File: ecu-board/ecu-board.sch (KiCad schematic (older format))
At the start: 12 parts, among them J1 MicroSquirt_connector, J3 MS_breakout_conn, U1 MPX4250AP

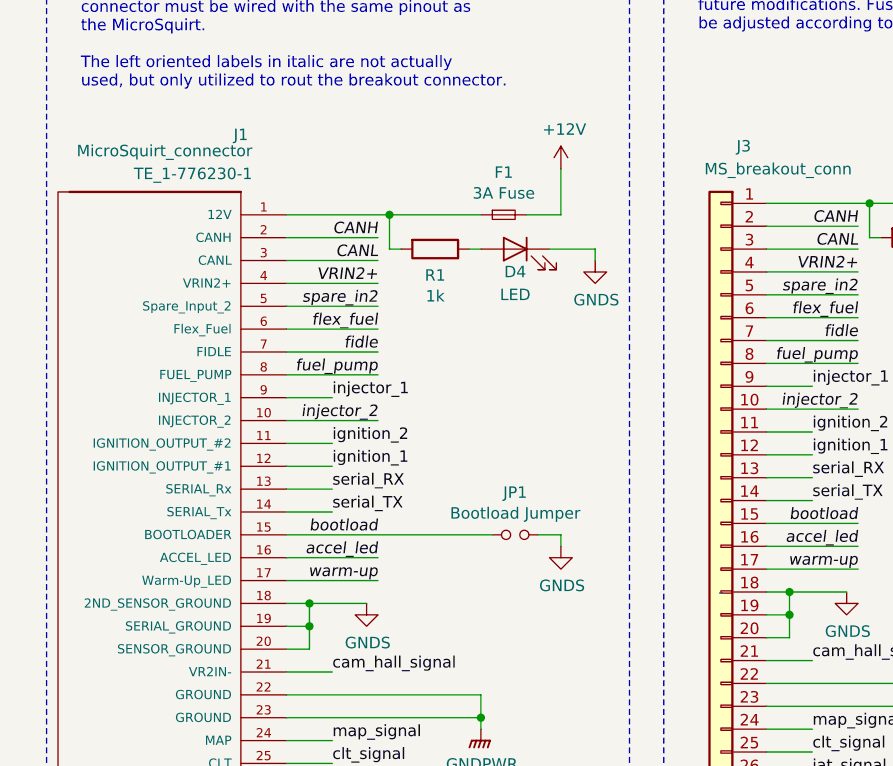
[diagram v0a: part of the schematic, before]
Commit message: Assign 2- and 3-pin terminal footprints.
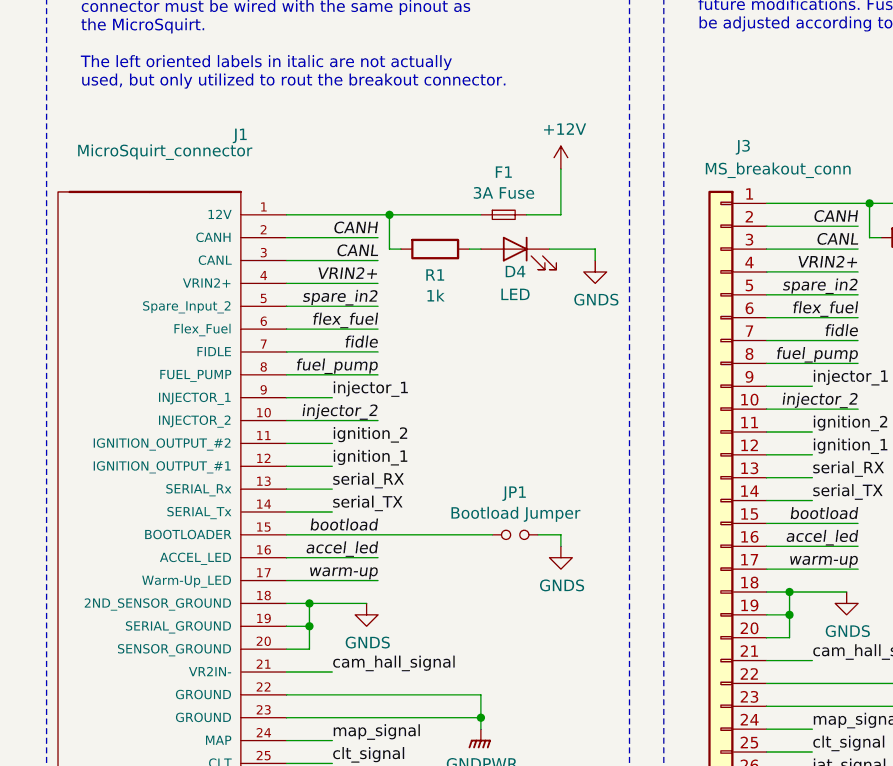
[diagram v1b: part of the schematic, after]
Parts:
- J1: footprint TE_1-776230-1 -> (none)
- J3: footprint - -> (none)
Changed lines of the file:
@@
 F 0 "J1" H 1650 6450 50  0000 C CNN
 F 1 "MicroSquirt_connector" H 1600 6350 50  0000 L BNN
-F 2 "TE_1-776230-1" H 1600 6250 50  0000 L BNN
+F 2 "" H 1600 6250 50  0000 L BNN
 F 3 "TE CONNECTIVITY" H 1850 4300 50  0001 L BNN
 	1    1850 4300
@@
 F 0 "J3" H 4050 6100 50  0000 C CNN
 F 1 "MS_breakout_conn" H 3900 6000 50  0000 C CNN
-F 2 "-" H 4150 4150 50  0000 C CNN
+F 2 "" H 4150 4150 50  0000 C CNN
 F 3 "https://www.phoenixcontact.com/gb/products/1791826" H 4150 4150 50  0001 C CNN
 F 4 "Phoenix Contact" H 4150 4150 50  0001 C CNN "Manufacturer"

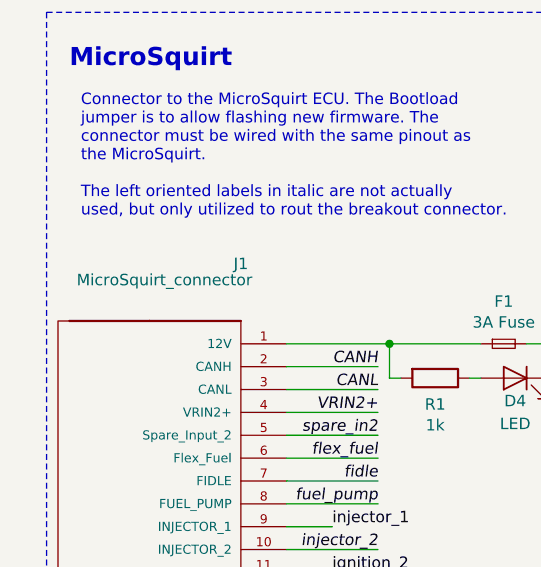
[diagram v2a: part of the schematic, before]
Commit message: Add component part no.
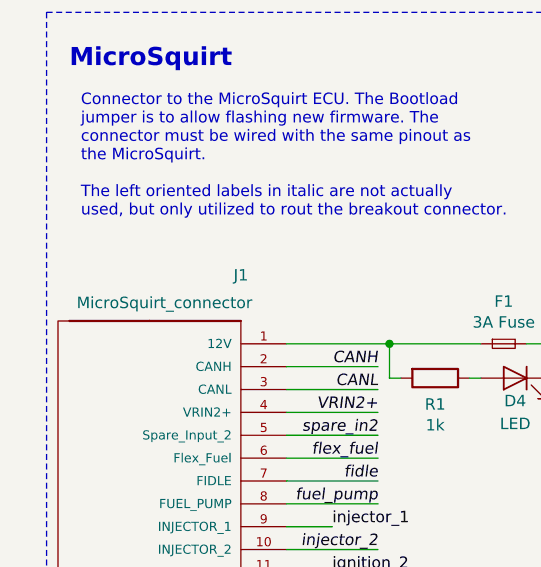
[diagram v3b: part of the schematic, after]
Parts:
- J1: Manufacturer (none) -> TE Connectivity; Part no. (none) -> 1-776230-1
- J3: Manufacturer Phoenix Contact -> (none)
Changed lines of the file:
@@
 U 1 1 5C598259
 P 1850 4300
-F 0 "J1" H 1650 6450 50  0000 C CNN
-F 1 "MicroSquirt_connector" H 1600 6350 50  0000 L BNN
+F 0 "J1" H 1650 6400 50  0000 C CNN
+F 1 "MicroSquirt_connector" H 1600 6250 50  0000 L BNN
 F 2 "" H 1600 6250 50  0001 L BNN
 F 3 "TE CONNECTIVITY" H 1850 4300 50  0001 L BNN
+F 4 "TE Connectivity" H 1850 4300 50  0001 C CNN "Manufacturer"
+F 5 "1-776230-1" H 1850 4300 50  0001 C CNN "Part no."
 	1    1850 4300
 	-1   0    0    -1
@@
 F 2 "" H 4150 4150 50  0001 C CNN
 F 3 "https://www.phoenixcontact.com/gb/products/1791826" H 4150 4150 50  0001 C CNN
-F 4 "Phoenix Contact" H 4150 4150 50  0001 C CNN "Manufacturer"
 	1    4150 4150
 	-1   0    0    -1

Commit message: Update LEDs.
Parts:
- D4, D5: Farnell 2251296 -> (none); Part no. (none) -> 3mm T-1
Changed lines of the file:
@@
 F 2 "LEDs:LED_D3.0mm" H 3250 2650 50  0001 C CNN
 F 3 "~" H 3250 2650 50  0001 C CNN
-F 4 "2251296" H 3250 2650 50  0001 C CNN "Farnell"
+F 4 "3mm T-1" H 3250 2650 50  0001 C CNN "Part no."
 	1    3250 2650
 	-1   0    0    -1
@@
 F 2 "LEDs:LED_D3.0mm" H 5350 2600 50  0001 C CNN
 F 3 "~" H 5350 2600 50  0001 C CNN
-F 4 "2251296" H 5350 2600 50  0001 C CNN "Farnell"
+F 4 "3mm T-1" H 5350 2600 50  0001 C CNN "Part no."
 	1    5350 2600
 	-1   0    0    -1

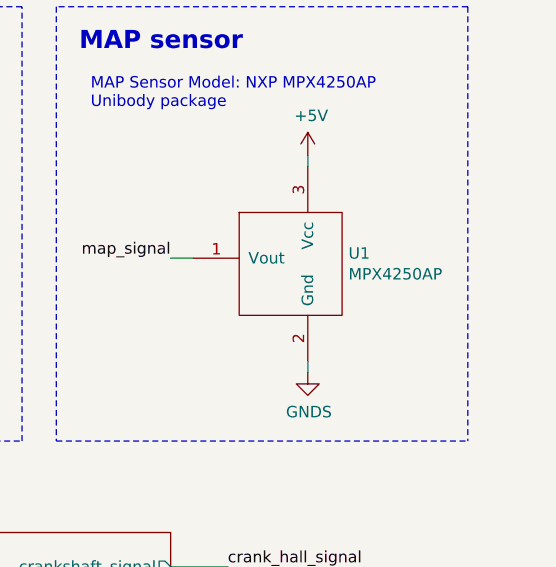
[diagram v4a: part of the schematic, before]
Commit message: Update MAP sensor value.
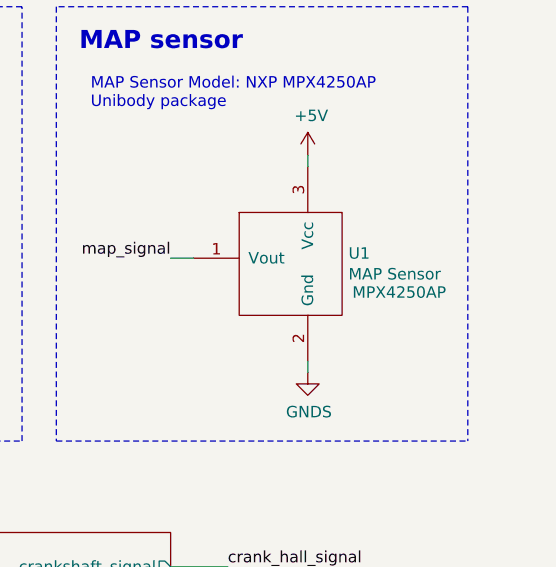
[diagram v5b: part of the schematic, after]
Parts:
- U1: value MPX4250AP -> MAP Sensor; Manufacturer (none) -> NXP; Part no. (none) -> MPX4250AP
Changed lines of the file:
@@
 AR Path="/5C731B59" Ref="U1"  Part="1"
 F 0 "U1" H 10122 1821 50  0000 R CNN
-F 1 "MPX4250AP" H 10122 1730 50  0000 R CNN
+F 1 "MAP Sensor" H 10122 1730 50  0000 R CNN
 F 2 "" H 10300 1700 50  0001 C CNN
 F 3 "" H 10300 1700 50  0001 C CNN
+F 4 "NXP" H 10300 1800 50  0001 C CNN "Manufacturer"
+F 5 "MPX4250AP" H 9900 1650 50  0000 C CNN "Part no."
 	1    10300 1800
 	-1   0    0    -1

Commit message: Update jumper info.
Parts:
- JP1: Farnell 1793581 -> (none); Part no. (none) -> 2x2.54mm Pin Header
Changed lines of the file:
@@
 F 2 "" H 3250 3900 50  0001 C CNN
 F 3 "~" H 3250 3900 50  0001 C CNN
-F 4 "1793581" H 3250 3900 50  0001 C CNN "Farnell"
+F 4 "2x2.54mm Pin Header" H 3250 3900 50  0001 C CNN "Part no."
 	1    3250 3900
 	1    0    0    -1

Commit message: Update fuse holder info.
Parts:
- F1, F2: Farnell 2292904 -> (none); Manufacturer (none) -> Littelfuse; Part no. (none) -> 01530008Z
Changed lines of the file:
@@
 F 2 "" H 3200 2500 50  0001 C CNN
 F 3 "~" H 3200 2500 50  0001 C CNN
-F 4 "2292904" H 3200 2500 50  0001 C CNN "Farnell"
+F 4 "Littelfuse" H 3200 2500 50  0001 C CNN "Manufacturer"
+F 5 "01530008Z" H 3200 2500 50  0001 C CNN "Part no."
 	1    3200 2500
 	1    0    0    -1
@@
 F 2 "" H 5300 2450 50  0001 C CNN
 F 3 "~" H 5300 2450 50  0001 C CNN
-F 4 "2292904" H 5300 2450 50  0001 C CNN "Farnell"
+F 4 "Littelfuse" H 5300 2450 50  0001 C CNN "Manufacturer"
+F 5 "01530008Z" H 5300 2450 50  0001 C CNN "Part no."
 	1    5300 2450
 	1    0    0    -1

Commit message: Assign resistor footprints.
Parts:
- R1, R2, R3, R4: footprint (none) -> Resistors_THT:R_Axial_DIN0309_L9.0mm_D3.2mm_P12.70mm_Horizontal
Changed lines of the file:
@@
 F 0 "R3" H 8070 1746 50  0000 L CNN
 F 1 "30k" H 8070 1655 50  0000 L CNN
-F 2 "" V 7930 1700 50  0001 C CNN
+F 2 "Resistors_THT:R_Axial_DIN0309_L9.0mm_D3.2mm_P12.70mm_Horizontal" V 7930 1700 50  0001 C CNN
 F 3 "~" H 8000 1700 50  0001 C CNN
 	1    8000 1700
@@
 F 0 "R4" H 8070 2146 50  0000 L CNN
 F 1 "30k" H 8070 2055 50  0000 L CNN
-F 2 "" V 7930 2100 50  0001 C CNN
+F 2 "Resistors_THT:R_Axial_DIN0309_L9.0mm_D3.2mm_P12.70mm_Horizontal" V 7930 2100 50  0001 C CNN
 F 3 "~" H 8000 2100 50  0001 C CNN
 	1    8000 2100
@@
 F 0 "R1" V 3015 2650 50  0000 C CNN
 F 1 "1k" V 3106 2650 50  0000 C CNN
-F 2 "" V 2830 2650 50  0001 C CNN
+F 2 "Resistors_THT:R_Axial_DIN0309_L9.0mm_D3.2mm_P12.70mm_Horizontal" V 2830 2650 50  0001 C CNN
 F 3 "~" H 2900 2650 50  0001 C CNN
 	1    2900 2650
@@
 F 0 "R2" V 5115 2600 50  0000 C CNN
 F 1 "1k" V 5206 2600 50  0000 C CNN
-F 2 "" V 4930 2600 50  0001 C CNN
+F 2 "Resistors_THT:R_Axial_DIN0309_L9.0mm_D3.2mm_P12.70mm_Horizontal" V 4930 2600 50  0001 C CNN
 F 3 "~" H 5000 2600 50  0001 C CNN
 	1    5000 2600
